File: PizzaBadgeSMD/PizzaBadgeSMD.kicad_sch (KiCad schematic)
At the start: 171 parts, among them Q1 NPN, Q2 NPN, Q3 NPN, Q4 NPN, Q5 NPN, Q6 NPN, Q7 NPN, Q8 NPN, SW1 RESET, SW2 Switch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

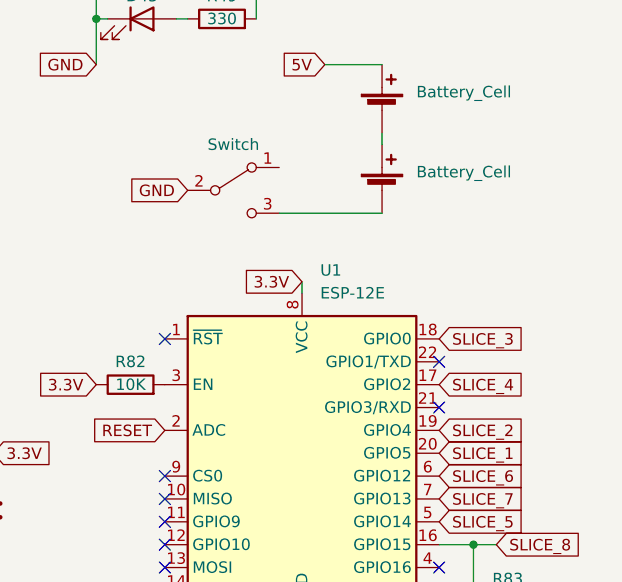
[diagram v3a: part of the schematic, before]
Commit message: update scheme and board on smd
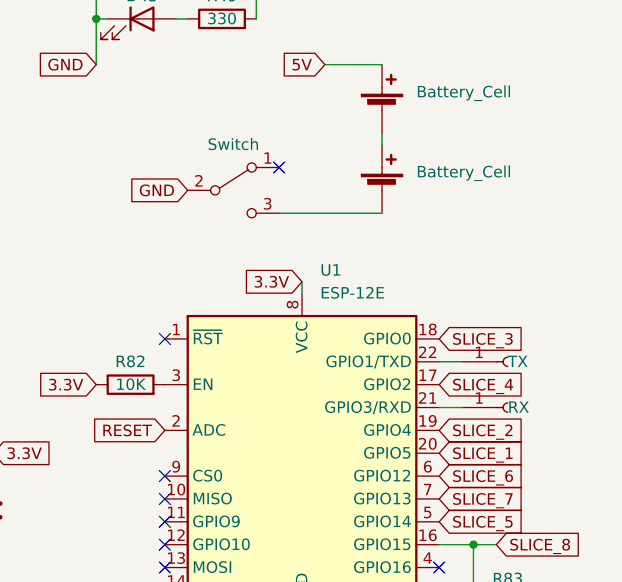
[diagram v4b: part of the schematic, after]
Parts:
- added J1: TX, TestPoint:TestPoint_Pad_2.0x2.0mm, symbol Connector:Conn_01x01_Female
- added J2: RX, TestPoint:TestPoint_Pad_2.0x2.0mm, symbol Connector:Conn_01x01_Female
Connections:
- net at U1.21 (GPIO3/RXD): now also J2.1 (Pin_1)
- net at U1.22 (GPIO1/TXD): now also J1.1 (Pin_1)
- no-connect marks 10 -> 9
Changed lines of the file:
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@@
   )
   (no_connect (at 234.95 148.59))
-  (no_connect (at 265.43 125.73))
   (no_connect (at 234.95 140.97))
   (no_connect (at 234.95 123.19))
@@
   (no_connect (at 234.95 146.05))
   (no_connect (at 234.95 138.43))
-  (no_connect (at 265.43 130.81))
+  (no_connect (at 247.65 104.14))
   (wire (pts (xy 227.33 54.61) (xy 227.33 62.23))
     (stroke (width 0) (type default) (color 0 0 0 0))
@@
     (stroke (width 0) (type default) (color 0 0 0 0))
   )
+  (wire (pts (xy 265.43 125.73) (xy 267.97 125.73))
+    (stroke (width 0) (type default) (color 0 0 0 0))
+  )
   (wire (pts (xy 121.92 44.45) (xy 121.92 52.07))
     (stroke (width 0) (type default) (color 0 0 0 0))
@@
     (stroke (width 0) (type default) (color 0 0 0 0))
   )
+  (wire (pts (xy 265.43 130.81) (xy 267.97 130.81))
+    (stroke (width 0) (type default) (color 0 0 0 0))
+  )
   (wire (pts (xy 78.74 44.45) (xy 80.01 44.45))
     (stroke (width 0) (type default) (color 0 0 0 0))
@@
     (pin "3")
   )
+  (symbol (lib_id "Connector:Conn_01x01_Female") (at 273.05 125.73 0) (unit 1)
+    (in_bom yes) (on_board yes)
+    (property "Reference" "J1" (id 0) (at 274.32 125.7299 0)
+      (effects (font (size 1.27 1.27)) (justify left) hide)
+    )
+    (property "Value" "TX" (id 1) (at 273.05 125.73 0)
+      (effects (font (size 1.27 1.27)) (justify left))
+    )
+    (property "Footprint" "TestPoint:TestPoint_Pad_2.0x2.0mm" (id 2) (at 273.05 125.73 0)
+      (effects (font (size 1.27 1.27)) hide)
+    )
+    (property "Datasheet" "~" (id 3) (at 273.05 125.73 0)
+      (effects (font (size 1.27 1.27)) hide)
+    )
+    (pin "1")
+  )
   (symbol (lib_id "Device:LED") (at 88.9 111.76 0) (unit 1)
     (in_bom yes) (on_board yes)
@@
     (pin "2")
   )
+  (symbol (lib_id "Connector:Conn_01x01_Female") (at 273.05 130.81 0) (unit 1)
+    (in_bom yes) (on_board yes)
+    (property "Reference" "J2" (id 0) (at 274.32 130.8099 0)
+      (effects (font (size 1.27 1.27)) (justify left) hide)
+    )
+    (property "Value" "RX" (id 1) (at 273.05 130.81 0)
+      (effects (font (size 1.27 1.27)) (justify left))
+    )
+    (property "Footprint" "TestPoint:TestPoint_Pad_2.0x2.0mm" (id 2) (at 273.05 130.81 0)
+      (effects (font (size 1.27 1.27)) hide)
+    )
+    (property "Datasheet" "~" (id 3) (at 273.05 130.81 0)
+      (effects (font (size 1.27 1.27)) hide)
+    )
+    (pin "1")
+  )
   (symbol (lib_id "Device:R") (at 184.15 36.83 90) (unit 1)
     (in_bom yes) (on_board yes)
@@
       (reference "D72") (unit 1) (value "LED") (footprint "LED_SMD:LED_0805_2012Metric")
     )
+    (path "/1984d29b-b18d-46ed-b777-6a38e9fc0fdc"
+      (reference "J1") (unit 1) (value "TX") (footprint "TestPoint:TestPoint_Pad_2.0x2.0mm")
+    )
+    (path "/80f59349-6b1c-4f08-b8f3-2a6aeaf5da71"
+      (reference "J2") (unit 1) (value "RX") (footprint "TestPoint:TestPoint_Pad_2.0x2.0mm")
+    )
     (path "/86e1da85-bdb0-4d78-b747-ecb447b1b842"
